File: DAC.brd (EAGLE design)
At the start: 97.8 x 55.9 mm, 73 parts, among them IC1 LM2662, IC2 PCM1793, IC3 OPA2134PA, J1 USBSMD, J2 RCJ-21XXMILL, U1 LDO-TPS78233, U2 PCM2707, Y1 12MHz/20pF

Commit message: Protection res
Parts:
- added LOGO1: LOGO-MANTIS, my:LOGO-MANTIS
- added R20, R21: 22, SparkFun-Resistors:AXIAL-0.4
- moved J2 1.27 mm to (94.0, 27.9)
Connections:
- new net N$100: C35.2, IC3.1, R17.P$2, R21.P$1
- new net N$101: C34.2, IC3.7, R14.P$2, R20.P$1
- net OUT_L: now also R21.P$2; no longer C35.2, IC3.1, R17.P$2
- net OUT_R: now also R20.P$2; no longer C34.2, IC3.7, R14.P$2
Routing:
- net OUT_L: track 21.6 -> 6.70 mm
- net N$101: track 0.00 -> 13.8 mm
- net N$100: track 0.00 -> 13.2 mm
- net OUT_R: track 18.2 -> 14.7 mm
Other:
- board size 97.8 x 55.9 mm -> 99.1 x 55.9 mm
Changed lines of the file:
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@@
 <board>
 <plain>
-<wire x1="0" y1="55.88" x2="97.79" y2="55.88" width="0.254" layer="20"/>
-<wire x1="97.79" y1="55.88" x2="97.79" y2="0" width="0.254" layer="20"/>
-<wire x1="97.79" y1="0" x2="0" y2="0" width="0.254" layer="20"/>
+<wire x1="0" y1="55.88" x2="99.06" y2="55.88" width="0.254" layer="20"/>
+<wire x1="99.06" y1="55.88" x2="99.06" y2="0" width="0.254" layer="20"/>
+<wire x1="99.06" y1="0" x2="0" y2="0" width="0.254" layer="20"/>
 <wire x1="0" y1="0" x2="0" y2="55.88" width="0.254" layer="20"/>
 <hole x="3.81" y="52.07" drill="3.2"/>
 <hole x="3.81" y="3.81" drill="3.2"/>
-<hole x="93.98" y="52.07" drill="3.2"/>
-<hole x="93.98" y="3.81" drill="3.2"/>
-<dimension x1="0" y1="55.88" x2="97.79" y2="55.88" x3="48.895" y3="59.69" textsize="1.27" layer="47" dtype="horizontal"/>
+<hole x="95.25" y="52.07" drill="3.2"/>
+<hole x="95.25" y="3.81" drill="3.2"/>
 <dimension x1="0" y1="0" x2="0" y2="55.88" x3="-3.81" y3="27.94" textsize="1.27" layer="47" dtype="vertical"/>
+<dimension x1="0" y1="55.88" x2="99.06" y2="55.88" x3="49.53" y3="59.69" textsize="1.27" layer="47" dtype="horizontal"/>
 </plain>
 <attributes>
@@
 <attribute name="VALUE" x="45.974" y="12.827" size="0.4064" layer="27" font="vector"/>
 </element>
-<element name="J2" library="my" package="RCJ-21-MILL" value="RCJ-21XXMILL" x="92.71" y="27.94" smashed="yes" rot="R270">
-<attribute name="NAME" x="95.25" y="30.48" size="1.27" layer="21" font="vector" ratio="15" rot="R270"/>
-<attribute name="VALUE" x="88.9" y="35.2425" size="1.27" layer="21" font="vector" ratio="15" rot="R270"/>
+<element name="J2" library="my" package="RCJ-21-MILL" value="RCJ-21XXMILL" x="93.98" y="27.94" smashed="yes" rot="R270">
+<attribute name="NAME" x="96.52" y="30.48" size="1.27" layer="21" font="vector" ratio="15" rot="R270"/>
+<attribute name="VALUE" x="90.17" y="35.2425" size="1.27" layer="21" font="vector" ratio="15" rot="R270"/>
 </element>
 <element name="C30" library="capacitor-wima" package="C5B4.5" value="4.7nF" x="81.28" y="52.07" smashed="yes" rot="R180">
@@
 </element>
 <element name="R17" library="SparkFun-Resistors" package="AXIAL-0.4" value="887" x="83.82" y="39.37" smashed="yes" rot="R270">
-<attribute name="NAME" x="85.4075" y="42.8625" size="0.8128" layer="25" font="vector" ratio="15" rot="R270"/>
+<attribute name="NAME" x="87.9475" y="42.8625" size="0.8128" layer="25" font="vector" ratio="15" rot="R270"/>
 <attribute name="VALUE" x="83.439" y="41.656" size="0.8128" layer="21" font="vector" ratio="15" rot="R270"/>
 </element>
@@
 </element>
 <element name="R9" library="SparkFun-Resistors" package="AXIAL-0.4" value="887" x="68.58" y="8.89" smashed="yes" rot="R180">
-<attribute name="NAME" x="71.755" y="6.985" size="0.8128" layer="25" font="vector" ratio="15" rot="R180"/>
+<attribute name="NAME" x="71.4375" y="11.43" size="0.8128" layer="25" font="vector" ratio="15" rot="R180"/>
 <attribute name="VALUE" x="70.866" y="9.271" size="0.8128" layer="21" font="vector" ratio="15" rot="R180"/>
 </element>
@@
 <attribute name="VALUE" x="67.437" y="31.496" size="0.4064" layer="27" font="vector" rot="R270"/>
 </element>
+<element name="R20" library="SparkFun-Resistors" package="AXIAL-0.4" value="22" x="86.36" y="16.51" smashed="yes" rot="R270">
+<attribute name="NAME" x="87.9475" y="15.5575" size="0.8128" layer="25" font="vector" ratio="15" rot="R270"/>
+<attribute name="VALUE" x="85.979" y="18.796" size="0.8128" layer="21" font="vector" ratio="15" rot="R270"/>
+</element>
+<element name="R21" library="SparkFun-Resistors" package="AXIAL-0.4" value="22" x="86.36" y="39.37" smashed="yes" rot="R90">
+<attribute name="NAME" x="84.455" y="36.195" size="0.8128" layer="25" font="vector" ratio="15" rot="R90"/>
+<attribute name="VALUE" x="86.741" y="37.084" size="0.8128" layer="21" font="vector" ratio="15" rot="R90"/>
+</element>
+<element name="LOGO1" library="my" package="LOGO-MANTIS" value="LOGO-MANTIS" x="60.96" y="30.48" rot="R270"/>
 </elements>
 <signals>
@@
 <polygon width="0.3048" layer="1" rank="2">
 <vertex x="0" y="55.88"/>
-<vertex x="97.79" y="55.88"/>
-<vertex x="97.79" y="0"/>
+<vertex x="99.06" y="55.88"/>
+<vertex x="99.06" y="0"/>
 <vertex x="0" y="0"/>
 </polygon>
 <polygon width="0.3048" layer="16" rank="2">
 <vertex x="0" y="55.88"/>
-<vertex x="97.79" y="55.88"/>
-<vertex x="97.79" y="0"/>
+<vertex x="99.06" y="55.88"/>
+<vertex x="99.06" y="0"/>
 <vertex x="0" y="0"/>
 </polygon>
@@
 <vertex x="46.6725" y="31.4325"/>
 <vertex x="46.6725" y="55.88"/>
-<vertex x="97.79" y="55.88"/>
-<vertex x="97.79" y="0"/>
+<vertex x="99.06" y="55.88"/>
+<vertex x="99.06" y="0"/>
 </polygon>
 <polygon width="0.3048" layer="16">
@@
 <vertex x="46.6725" y="31.4325"/>
 <vertex x="46.6725" y="55.88"/>
-<vertex x="97.79" y="55.88"/>
-<vertex x="97.79" y="0"/>
+<vertex x="99.06" y="55.88"/>
+<vertex x="99.06" y="0"/>
 </polygon>
 <contactref element="GB2" pad="P$2.2"/>
@@
 <via x="85.09" y="53.34" extent="1-16" drill="0.5"/>
 <via x="90.17" y="53.34" extent="1-16" drill="0.5"/>
-<via x="95.25" y="46.99" extent="1-16" drill="0.5"/>
-<via x="95.25" y="43.18" extent="1-16" drill="0.5"/>
-<via x="95.25" y="12.7" extent="1-16" drill="0.5"/>
-<via x="95.25" y="7.62" extent="1-16" drill="0.5"/>
+<via x="96.52" y="46.99" extent="1-16" drill="0.5"/>
+<via x="96.52" y="43.18" extent="1-16" drill="0.5"/>
+<via x="96.52" y="12.7" extent="1-16" drill="0.5"/>
+<via x="96.52" y="7.62" extent="1-16" drill="0.5"/>
 <via x="91.44" y="2.54" extent="1-16" drill="0.5"/>
 <via x="86.36" y="2.54" extent="1-16" drill="0.5"/>
@@
 </signal>
 <signal name="OUT_L" class="2">
-<contactref element="IC3" pad="1"/>
-<contactref element="C35" pad="2"/>
-<contactref element="R17" pad="P$2"/>
 <contactref element="J2" pad="4"/>
-<wire x1="78.74" y1="31.75" x2="80.01" y2="31.75" width="0.4064" layer="1"/>
-<wire x1="80.01" y1="31.75" x2="83.82" y2="31.75" width="0.4064" layer="1"/>
-<wire x1="83.82" y1="31.75" x2="87.63" y2="35.56" width="0.4064" layer="1" curve="90"/>
-<wire x1="87.63" y1="35.56" x2="87.63" y2="38.61" width="0.4064" layer="1"/>
-<wire x1="87.63" y1="38.61" x2="87.96" y2="38.94" width="0.4064" layer="1" curve="-90"/>
-<wire x1="83.82" y1="34.29" x2="83.82" y2="31.75" width="0.4064" layer="1"/>
-<wire x1="80.01" y1="36.83" x2="80.01" y2="31.75" width="0.4064" layer="1"/>
+<contactref element="R21" pad="P$2"/>
+<wire x1="86.36" y1="44.45" x2="89.23" y2="41.58" width="0.4064" layer="1" curve="-90"/>
+<wire x1="89.23" y1="41.58" x2="89.23" y2="38.94" width="0.4064" layer="1"/>
 </signal>
 <signal name="OUT_R" class="2">
-<contactref element="C34" pad="2"/>
-<contactref element="R14" pad="P$2"/>
-<contactref element="IC3" pad="7"/>
 <contactref element="J2" pad="2"/>
-<wire x1="76.2" y1="24.13" x2="77.47" y2="22.86" width="0.4064" layer="1" curve="90"/>
-<wire x1="77.47" y1="22.86" x2="80.01" y2="22.86" width="0.4064" layer="1"/>
-<wire x1="80.01" y1="22.86" x2="83.82" y2="22.86" width="0.4064" layer="1"/>
-<wire x1="83.82" y1="22.86" x2="85.88" y2="22.86" width="0.4064" layer="1"/>
-<wire x1="85.88" y1="22.86" x2="87.96" y2="24.94" width="0.4064" layer="1" curve="90"/>
-<wire x1="83.82" y1="21.59" x2="83.82" y2="22.86" width="0.4064" layer="1"/>
-<wire x1="80.01" y1="19.05" x2="80.01" y2="22.86" width="0.4064" layer="1"/>
+<contactref element="R20" pad="P$2"/>
+<wire x1="86.36" y1="11.43" x2="89.23" y2="14.3" width="0.4064" layer="1" curve="90"/>
+<wire x1="89.23" y1="14.3" x2="89.23" y2="24.94" width="0.4064" layer="1"/>
 </signal>
 <signal name="OPL-" class="2">
@@
 <wire x1="71.12" y1="3.81" x2="78.74" y2="3.81" width="0.4064" layer="1"/>
 </signal>
+<signal name="N$100" class="2">
+<contactref element="IC3" pad="1"/>
+<contactref element="C35" pad="2"/>
+<contactref element="R17" pad="P$2"/>
+<contactref element="R21" pad="P$1"/>
+<wire x1="78.74" y1="31.75" x2="78.74" y2="34.29" width="0.4064" layer="1"/>
+<wire x1="78.74" y1="34.29" x2="78.74" y2="35.56" width="0.4064" layer="1"/>
+<wire x1="78.74" y1="35.56" x2="80.01" y2="36.83" width="0.4064" layer="1" curve="-90"/>
+<wire x1="86.36" y1="34.29" x2="83.82" y2="34.29" width="0.4064" layer="1"/>
+<wire x1="83.82" y1="34.29" x2="78.74" y2="34.29" width="0.4064" layer="1"/>
+</signal>
+<signal name="N$101" class="2">
+<contactref element="C34" pad="2"/>
+<contactref element="R14" pad="P$2"/>
+<contactref element="IC3" pad="7"/>
+<contactref element="R20" pad="P$1"/>
+<wire x1="76.2" y1="24.13" x2="77.47" y2="22.86" width="0.4064" layer="1" curve="90"/>
+<wire x1="77.47" y1="22.86" x2="78.74" y2="22.86" width="0.4064" layer="1"/>
+<wire x1="78.74" y1="22.86" x2="80.01" y2="21.59" width="0.4064" layer="1" curve="-90"/>
+<wire x1="80.01" y1="21.59" x2="80.01" y2="19.05" width="0.4064" layer="1"/>
+<wire x1="86.36" y1="21.59" x2="83.82" y2="21.59" width="0.4064" layer="1"/>
+<wire x1="83.82" y1="21.59" x2="80.01" y2="21.59" width="0.4064" layer="1"/>
+</signal>
 </signals>

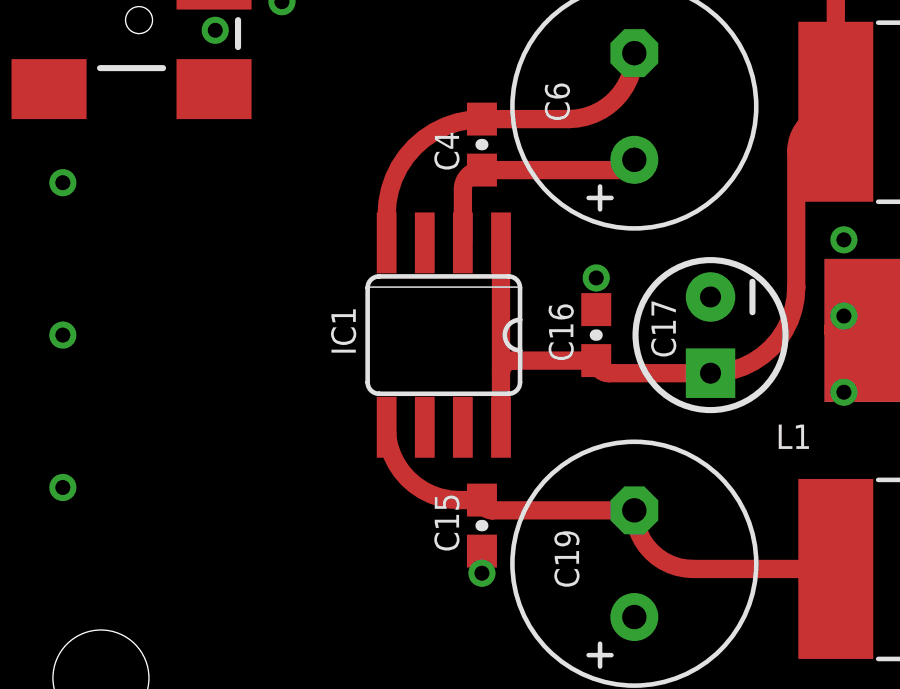
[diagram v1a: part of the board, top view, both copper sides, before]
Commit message: Some packages updated
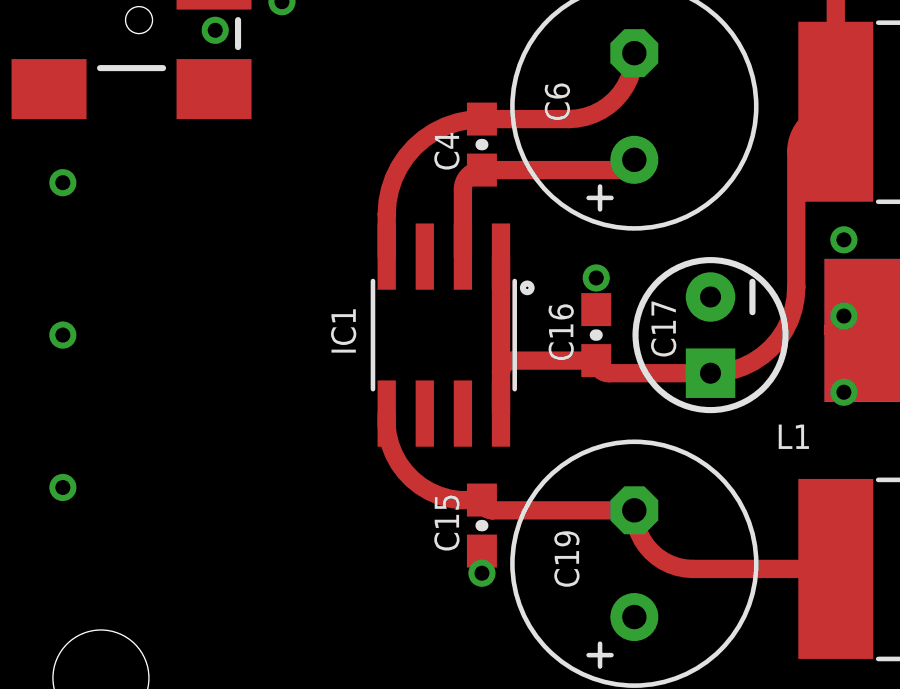
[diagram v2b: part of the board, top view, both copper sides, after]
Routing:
- net VCC: track 97.6 -> 96.7 mm
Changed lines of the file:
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@@
 <wire x1="24.13" y1="13.97" x2="20.74" y2="13.97" width="0.6096" layer="1"/>
 <wire x1="20.74" y1="13.97" x2="20.32" y2="14.39" width="0.6096" layer="1" curve="-90"/>
-<wire x1="17.145" y1="18.3134" x2="17.145" y2="13.97" width="0.6096" layer="1"/>
-<wire x1="17.145" y1="13.97" x2="17.145" y2="12.1666" width="0.6096" layer="1"/>
+<wire x1="17.145" y1="17.8562" x2="17.145" y2="13.97" width="0.6096" layer="1"/>
+<wire x1="17.145" y1="13.97" x2="17.145" y2="12.6238" width="0.6096" layer="1"/>
 <wire x1="20.32" y1="14.39" x2="17.565" y2="14.39" width="0.6096" layer="1"/>
 <wire x1="17.565" y1="14.39" x2="17.145" y2="13.97" width="0.6096" layer="1" curve="90"/>
@@
 <contactref element="C6" pad="-"/>
 <contactref element="C4" pad="2"/>
-<wire x1="13.335" y1="18.3134" x2="13.335" y2="19.265" width="0.6096" layer="1"/>
+<wire x1="13.335" y1="17.8562" x2="13.335" y2="19.265" width="0.6096" layer="1"/>
 <wire x1="13.335" y1="19.265" x2="16.51" y2="22.44" width="0.6096" layer="1" curve="-90"/>
 <wire x1="16.51" y1="22.44" x2="19.392" y2="22.44" width="0.6096" layer="1"/>
@@
 <contactref element="C6" pad="+"/>
 <contactref element="C4" pad="1"/>
-<wire x1="15.875" y1="18.3134" x2="15.875" y2="20.105" width="0.6096" layer="1"/>
+<wire x1="15.875" y1="17.8562" x2="15.875" y2="20.105" width="0.6096" layer="1"/>
 <wire x1="15.875" y1="20.105" x2="16.51" y2="20.74" width="0.6096" layer="1" curve="-90"/>
 <wire x1="16.51" y1="20.74" x2="21.248" y2="20.74" width="0.6096" layer="1"/>
@@
 <contactref element="C15" pad="2"/>
 <contactref element="L1" pad="1"/>
-<wire x1="13.335" y1="12.1666" x2="15.7616" y2="9.74" width="0.6096" layer="1" curve="90"/>
+<wire x1="13.335" y1="12.6238" x2="15.7616" y2="9.74" width="0.6096" layer="1" curve="90"/>
 <wire x1="15.7616" y1="9.74" x2="16.51" y2="9.74" width="0.6096" layer="1"/>
 <wire x1="16.51" y1="9.74" x2="16.852" y2="9.398" width="0.6096" layer="1" curve="90"/>

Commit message: Phone out
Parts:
- added C43, C44: 100pF, SparkFun-Capacitors:CAP-PTH-SMALL
- added C45, C46: 1.0uF, SparkFun-Capacitors:0603-CAP
- added IC4: LMH6643, my:SO08
- added J3: (no value), SparkFun-Connectors:STEREOJACK2.5MM_STEREOJACK2.5MM
- added R22: TD90, my:PTD902
- added R23, R26: 3.3k, SparkFun-Resistors:AXIAL-0.4
- added R24, R27: 1.8k, SparkFun-Resistors:AXIAL-0.4
- moved R20 67.5 mm to (41.9, 67.3), turned to 90 degrees
- moved J2 53.6 mm to (62.2, 71.1), turned to 0 degrees
- moved R21 49.3 mm to (45.7, 67.3)
- moved J1 45.4 mm to (19.1, 71.1), turned to 270 degrees
- moved LOGO1 45.2 mm to (33.0, 66.0), turned to 0 degrees
- moved R3 23.5 mm to (12.7, 60.3)
- moved R4 23.2 mm to (10.2, 62.2), turned to 0 degrees
- moved R5 20.4 mm to (15.2, 62.2), turned to 0 degrees
- moved R13 13.5 mm to (57.1, 49.5)
- moved R12 13.5 mm to (57.1, 26.7)
- moved C1 13.5 mm to (29.2, 45.1)
- moved C14 13.5 mm to (20.3, 58.4)
- moved C21 13.5 mm to (26.7, 33.0)
- moved C26 13.5 mm to (35.6, 45.1)
- moved C35 13.5 mm to (71.1, 49.5)
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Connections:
- net N$6 renamed D+*
- net N$7 renamed D-*
- removed net N$100: C35.2, IC3.1, R17.P$2, R21.P$1
- removed net N$101: C34.2, IC3.7, R14.P$2, R20.P$1
- new net HP_L: C43.1, IC4.1, J3.SHIELD, R23.P$2
- new net HP_R: C44.1, IC4.7, J3.TIP, R26.P$2
- new net N$12: IC4.3, R22.R1.2
- new net N$14: C43.2, IC4.2, R23.P$1, R24.P$2
- new net N$15: IC4.5, R22.R2.2
- new net N$19: C44.2, IC4.6, R26.P$1, R27.P$2
- new net OUT_L*: C35.2, IC3.1, R17.P$2, R21.P$1, R22.R1.3
- new net OUT_R*: C34.2, IC3.7, R14.P$2, R20.P$1, R22.R2.3
- net +5V: now also C46.1, IC4.8
- net -5V: now also C45.1, IC4.4
- net AGND: now also C45.2, C46.2, J3.RING1, R22.R1.1, R22.R2.1, R24.P$1, R27.P$1
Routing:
- net OUT_L*: track 0.00 -> 91.1 mm, vias 0 -> 1
- net OUT_R*: track 0.00 -> 79.8 mm, vias 0 -> 1
- net HP_R: track 0.00 -> 38.1 mm, vias 0 -> 1
- net +5V: track 90.2 -> 123.8 mm, vias 1 -> 4
- net HP_L: track 0.00 -> 28.7 mm
- net N$12: track 0.00 -> 27.8 mm, vias 0 -> 1
- net N$15: track 0.00 -> 26.2 mm
- net -5V: track 63.3 -> 84.3 mm, vias 4 -> 5
- net N$19: track 0.00 -> 18.1 mm
- net N$101: track 13.8 -> 0.00 mm
- net N$100: track 13.2 -> 0.00 mm
- net OUT_R: track 14.7 -> 27.7 mm
- net N$14: track 0.00 -> 12.0 mm
- net VCC: track 96.7 -> 88.6 mm, vias 2 -> 0
- net D-: track 16.0 -> 7.95 mm
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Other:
- board size 99.1 x 55.9 mm -> 81.3 x 76.2 mm
